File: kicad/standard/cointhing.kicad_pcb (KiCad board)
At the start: 2 copper layers, 35 x 34 mm, 27 parts, among them J1 USB_B_Micro, Q1 PUMX1, Q2 S8050_J3Y, U1 ESP-12E, U2 CP2102-GMR_NRND, U3 BL8565, U4 74AHC1G08

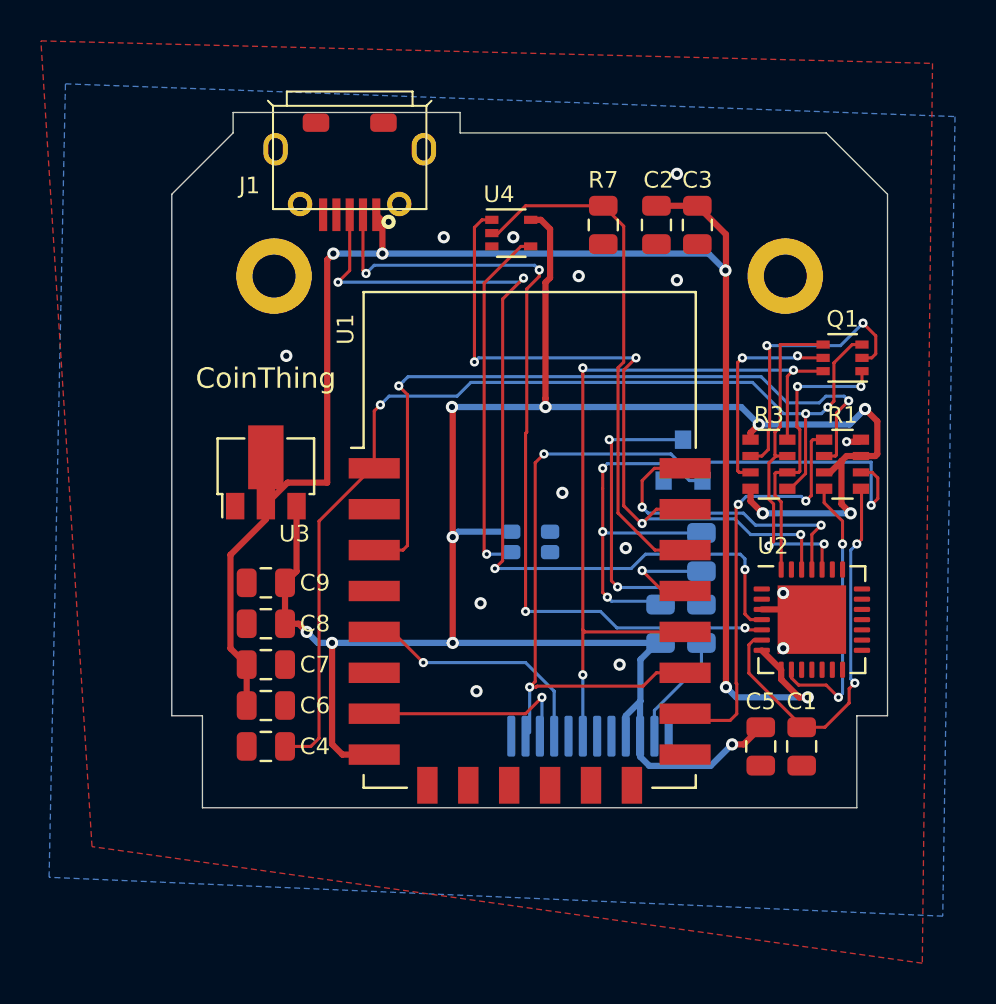
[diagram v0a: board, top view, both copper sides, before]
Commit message: PCB rev.D
All components on top layer
CP2102 <> CP2104
Prepared for SMT assembly
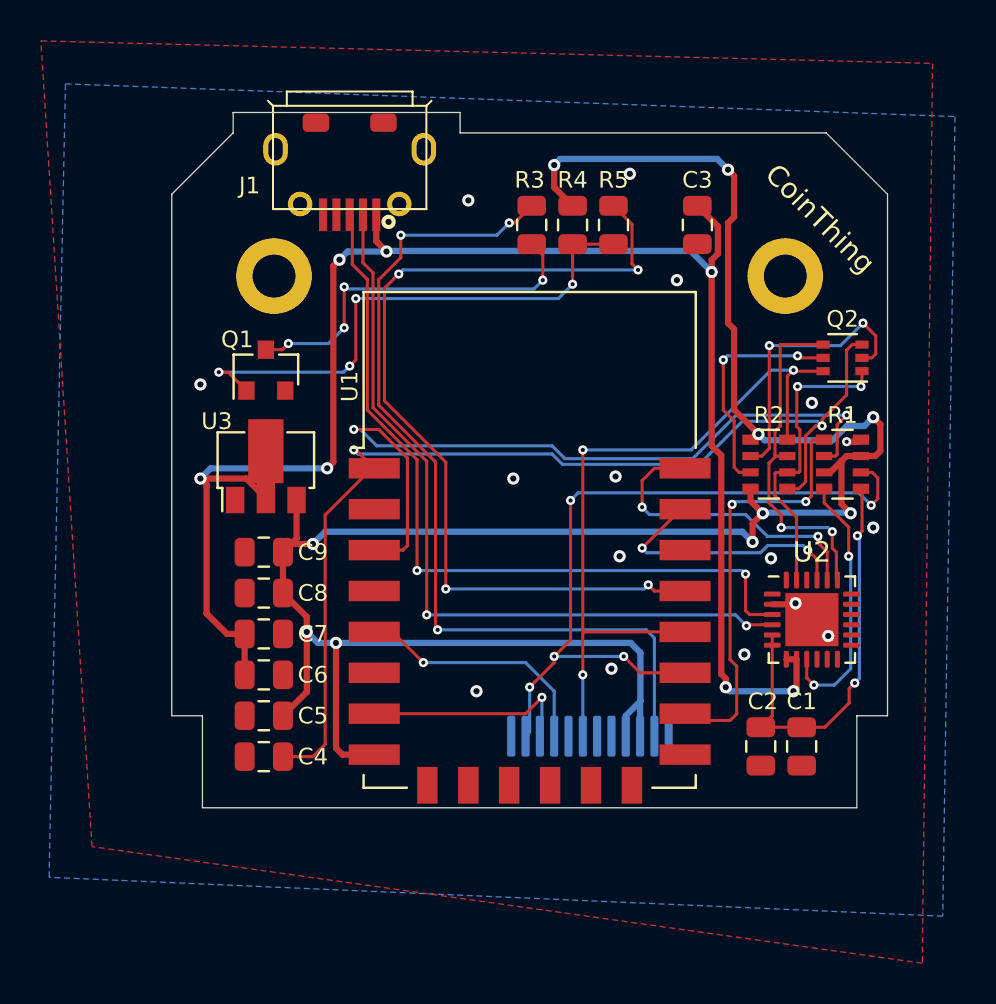
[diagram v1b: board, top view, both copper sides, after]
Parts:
- removed the D1 at (162.5, 76.0)
- removed R7: 10k, Resistor_SMD:R_0805_2012Metric
- removed U4: 74AHC1G08, Package_TO_SOT_SMD:SOT-353_SC-70-5
- Q1: renamed from Q2; moved to F.Cu
- Q2: renamed from Q1; value PUMX1 -> PMBT2222AYSX
- R3: renamed from R4; moved to F.Cu
- R4: renamed from R5; moved to F.Cu
- R5: renamed from R6; moved to F.Cu
- U2: value CP2102-GMR_NRND -> CP2104; footprint Package_DFN_QFN:QFN-28-1EP_5x5mm_P0.5mm_EP3.35x3.35mm -> Package_DFN_QFN:QFN-24-1EP_4x4mm_P0.5mm_EP2.6x2.6mm
- moved C2 26.0 mm to (173.8, 86.0)
- moved C5 24.3 mm to (149.5, 84.5), turned to 180 degrees
- moved R3 21.2 mm to (162.6, 60.5), turned to 270 degrees
- moved Q1 20.9 mm to (149.6, 67.6)
- moved R4 20.0 mm to (164.6, 60.5), turned to 90 degrees
- moved R5 16.6 mm to (166.6, 60.5), turned to 90 degrees
- moved C6 1.50 mm to (149.5, 82.5)
- moved C7 1.50 mm to (149.5, 80.5)
- moved C8 1.50 mm to (149.5, 78.5)
- moved C9 1.50 mm to (149.5, 76.5)
- moved C4 0.51 mm to (149.5, 86.5)
- moved U3 0.30 mm to (149.6, 72.3)
- renumbered D2 to D1, R3 to R2
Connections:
- C2 pad 1: VBUS -> /VDD
- U1 pad 20: /GPIO5 -> (no net)
- U2 pad 19: (no net) -> /RTS
- U2 pad 2: (no net) -> GND
- U2 pad 20: (no net) -> /RxD
- U2 pad 21: (no net) -> /TxD
- U2 pad 23: (no net) -> /DTR
- U2 pad 24: /RTS -> (no net)
- U2 pad 25: /RxD -> GND
- U2 pad 3: GND -> /D+
- U2 pad 4: /D+ -> /D-
- U2 pad 5: /D- -> /VDD
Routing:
- net /TFT_BL: track 5.46 -> 44.3 mm, vias 1 -> 4
- net /LEDK: track 5.52 -> 43.5 mm, vias 0 -> 3
- net /GPIO5: track 25.6 -> 0.00 mm
- net /TxD: track 36.6 -> 13.0 mm, vias 4 -> 2
- net Net-(D1-Pad3): track 17.6 -> 0.00 mm, vias 1 -> 0
- net Net-(Q1-Pad1): track 19.5 -> 26.5 mm, vias 3 -> 4
- net /~TFT_RES: track 42.7 -> 36.7 mm, vias 3 -> 5
- net /D+: track 43.8 -> 38.2 mm, vias 4 -> 2
- net +3V3: track 107.0 -> 112.1 mm, vias 11 -> 10
- net Net-(Q1-Pad3): track 15.5 -> 18.2 mm, vias 2 -> 4
- net /D-: track 40.6 -> 38.0 mm, vias 4 -> 2
- net /GPIO0: track 38.4 -> 36.0 mm
- net Net-(R1-Pad6): track 36.2 -> 37.5 mm
- net VBUS: track 81.0 -> 82.2 mm, vias 5 -> 7
- net Net-(Q2-Pad5): track 10.3 -> 11.4 mm
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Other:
- board text added: "CoinThing barn53 rev.D 04/21"
- board text removed: "CoinThing barn53 rev.C 02/21"

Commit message: Update cointhing.kicad_pcb
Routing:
- net /TFT_BL: track 44.3 -> 46.4 mm
- net /LEDK: track 43.5 -> 45.5 mm
- net VBUS: track 82.2 -> 84.0 mm, vias 7 -> 5
- net /GPIO0: track 36.0 -> 37.4 mm
- net Net-(R1-Pad6): track 37.5 -> 38.8 mm
- net /D-: track 38.0 -> 38.9 mm
- net /D+: track 38.2 -> 38.9 mm
- net GND: vias 16 -> 18

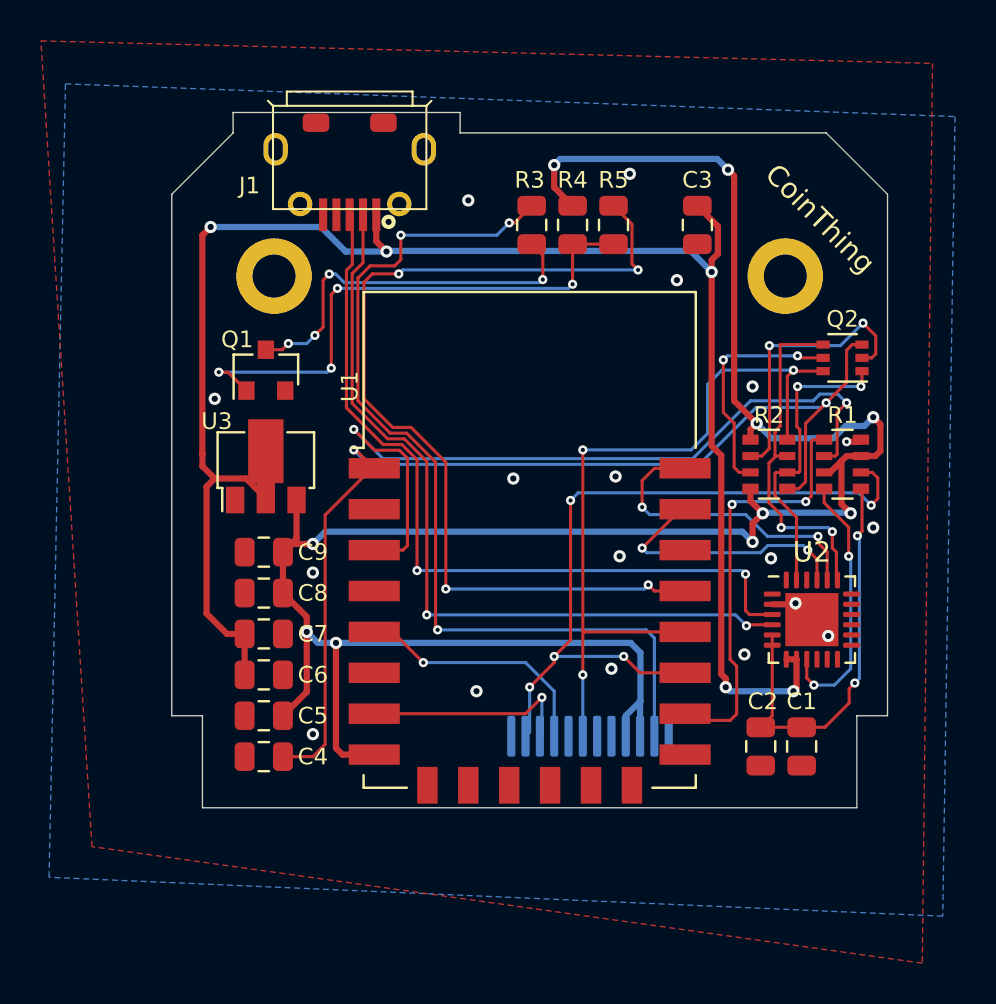
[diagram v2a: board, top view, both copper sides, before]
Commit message: PCB rev.E back to CP2102
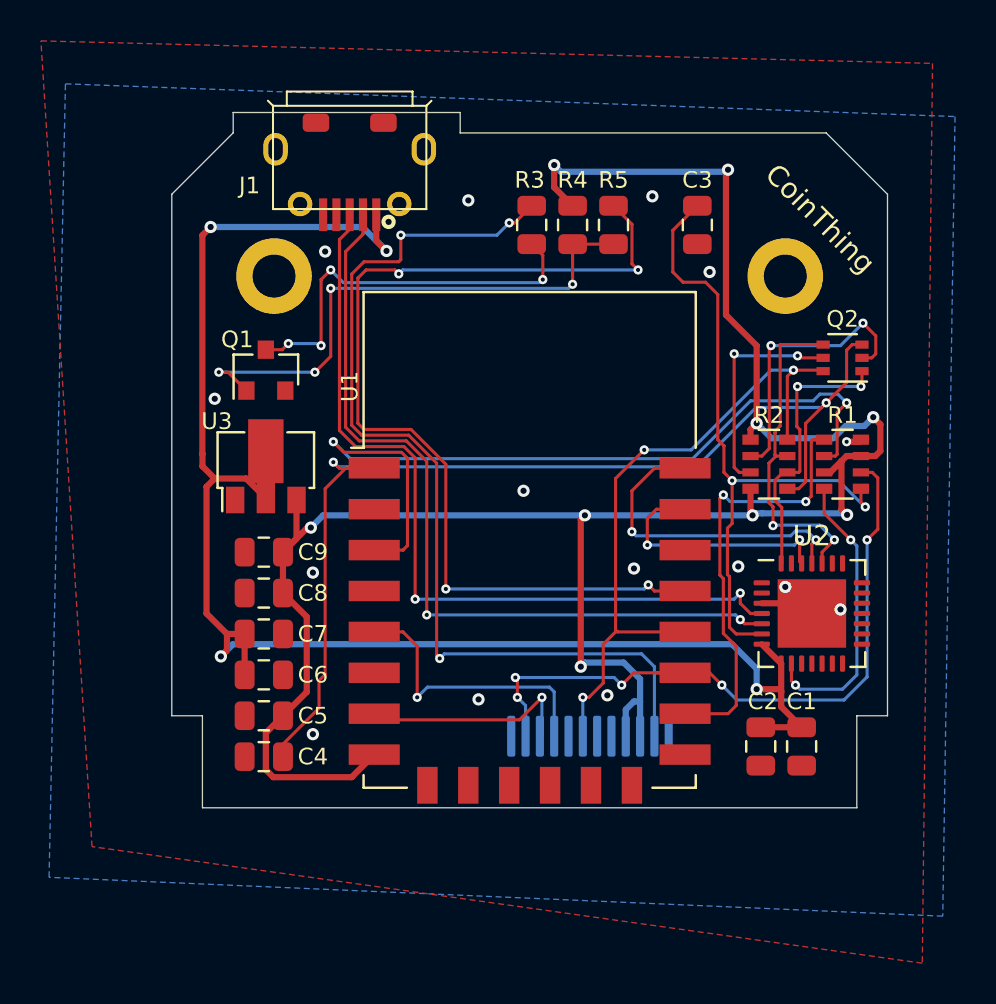
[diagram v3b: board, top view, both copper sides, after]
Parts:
- Q2: value PMBT2222AYSX -> PMBT2222AYS
- U2: value CP2104 -> CP2102-GMR_NRND; footprint Package_DFN_QFN:QFN-24-1EP_4x4mm_P0.5mm_EP2.6x2.6mm -> Package_DFN_QFN:QFN-28-1EP_5x5mm_P0.5mm_EP3.35x3.35mm
- moved U2 0.30 mm to (176.3, 79.5)
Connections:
- C1 pad 1: /VDD -> VBUS
- C2 pad 1: /VDD -> VBUS
- C3 pad 1: VBUS -> /VDD
- U2 pad 19: /RTS -> (no net)
- U2 pad 2: GND -> (no net)
- U2 pad 20: /RxD -> (no net)
- U2 pad 21: /TxD -> (no net)
- U2 pad 23: /DTR -> (no net)
- U2 pad 24: (no net) -> /RTS
- U2 pad 25: GND -> /RxD
- U2 pad 3: /D+ -> GND
- U2 pad 4: /D- -> /D+
- U2 pad 5: /VDD -> /D-
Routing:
- net /VDD: track 20.4 -> 32.8 mm
- net VBUS: track 84.0 -> 75.0 mm, vias 5 -> 4
- net +3V3: track 112.0 -> 105.4 mm, vias 10 -> 9
- net /GPIO0: track 37.4 -> 32.8 mm
- net /~TFT_RES: track 36.7 -> 34.0 mm
- net /TFT_SCL: track 12.2 -> 14.1 mm
- net /LEDK: track 45.5 -> 47.1 mm
- net /TFT_BL: track 46.4 -> 47.9 mm
- net Net-(R1-Pad6): track 38.8 -> 40.3 mm
- net /~Reset: track 52.0 -> 53.5 mm
- net Net-(R1-Pad8): track 12.9 -> 14.3 mm
- net /DTR: track 15.0 -> 13.7 mm
- net /TxD: track 13.0 -> 12.1 mm
- net /D+: track 38.9 -> 39.8 mm
- net Net-(Q1-Pad3): track 18.6 -> 19.4 mm
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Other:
- board text added: "CoinThing barn53 rev.E 05/21"
- board text removed: "CoinThing barn53 rev.D 04/21"
